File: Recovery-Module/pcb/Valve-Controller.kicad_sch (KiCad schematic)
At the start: 0 parts

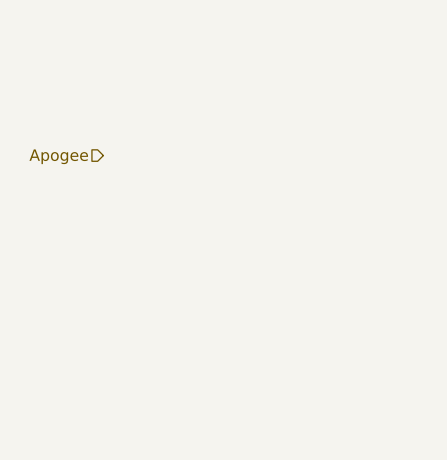
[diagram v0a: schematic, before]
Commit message: Draft of valve schematic
without load resistor and mosfet, waiting for valve to be ordered
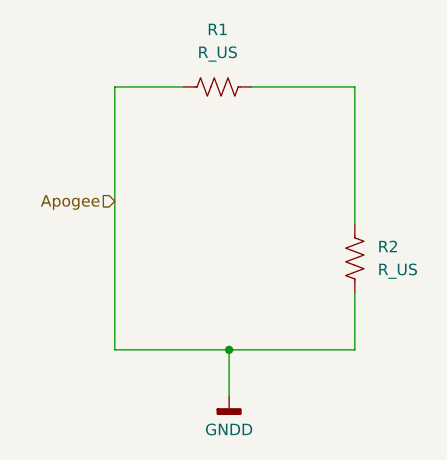
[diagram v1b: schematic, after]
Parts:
- added R1, R2: R_US, symbol Device:R_US
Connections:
- new net: R1.1, R2.1
- new net GNDD: R1.2, R2.2
